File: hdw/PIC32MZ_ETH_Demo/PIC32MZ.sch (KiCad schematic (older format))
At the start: 1 part

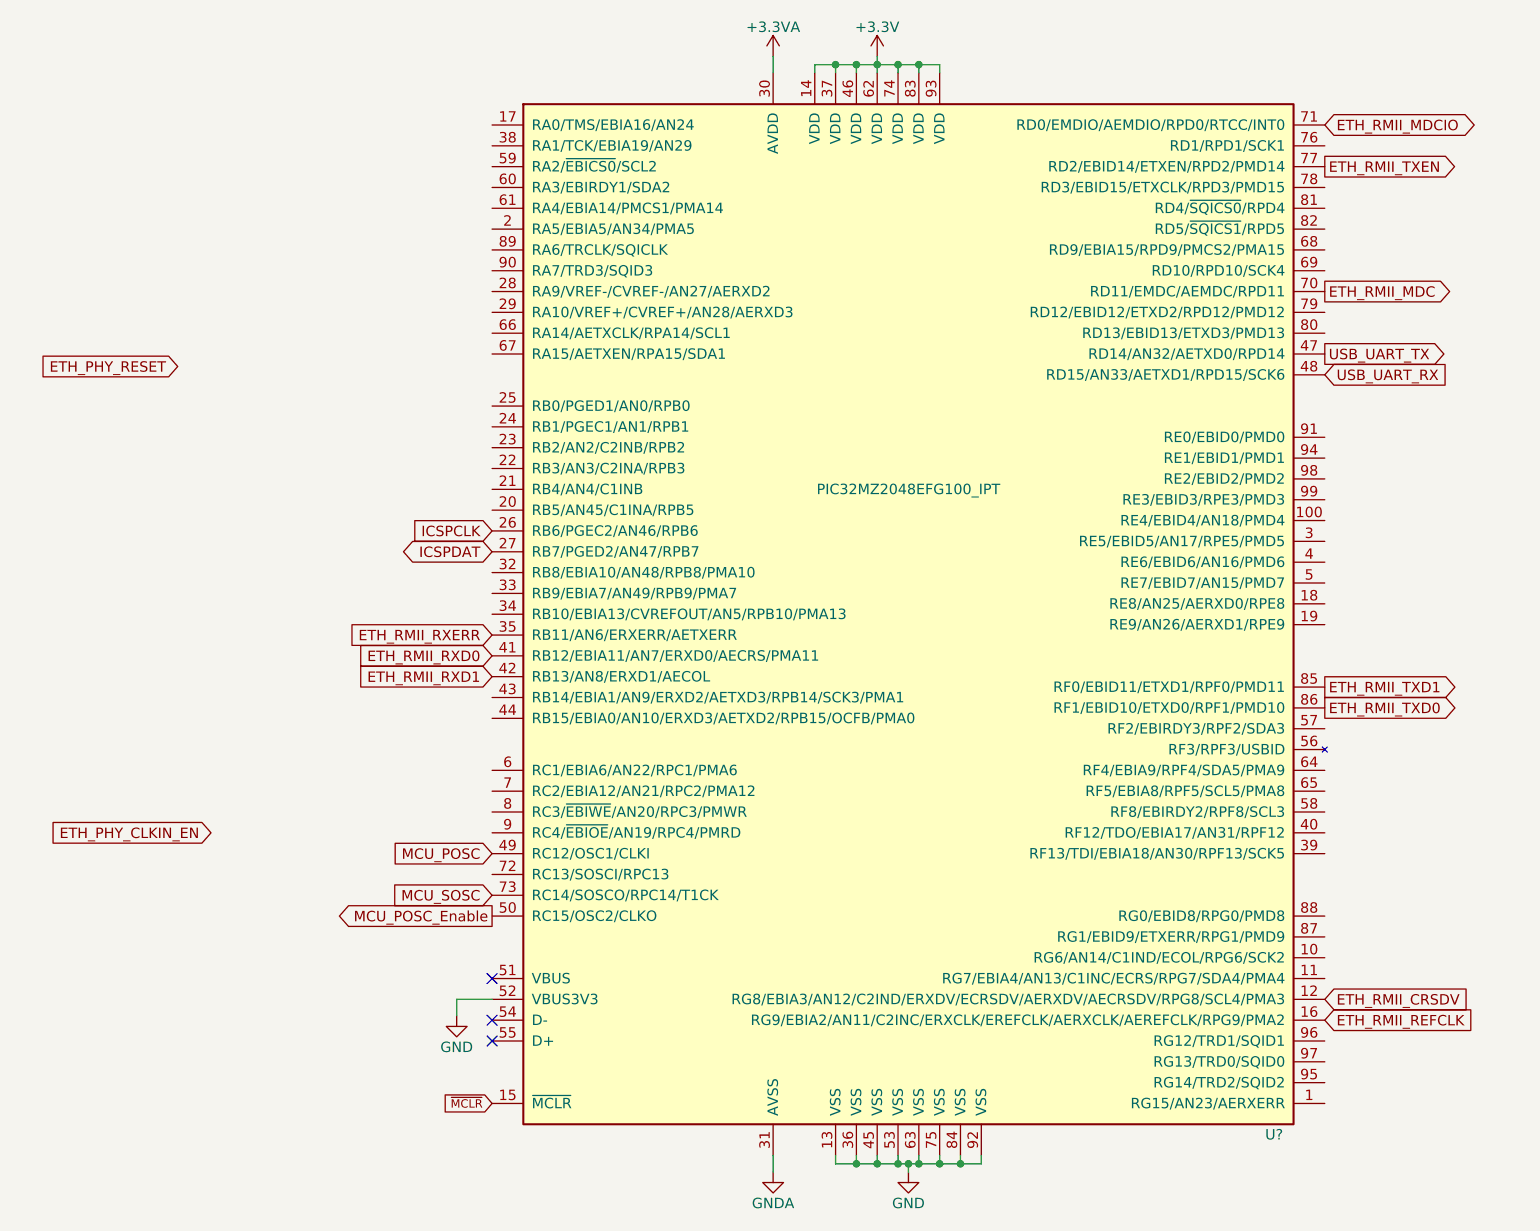
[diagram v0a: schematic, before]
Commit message: More schematic tweaks, followed PHY design guide
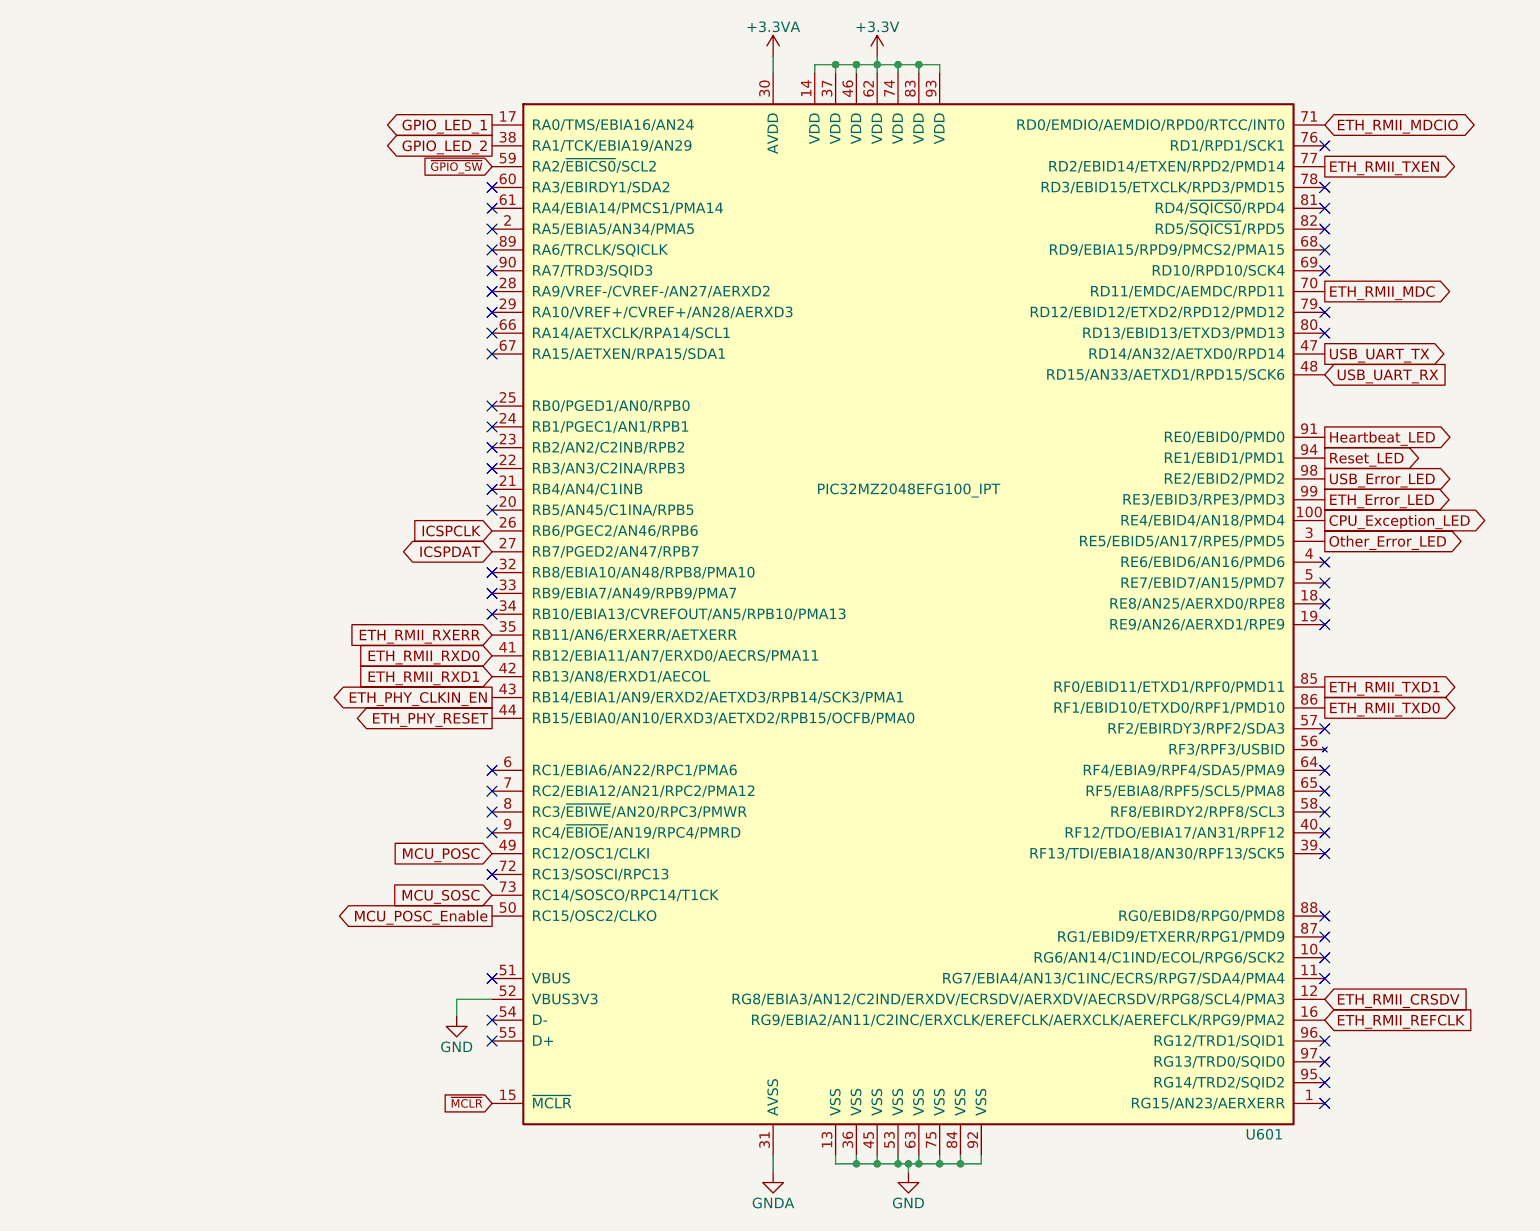
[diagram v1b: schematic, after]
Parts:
- gave numbers to parts that had none: 1
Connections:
- net ETH_PHY_CLKIN_EN: now also U601.43 (RB14/EBIA1/AN9/ERXD2/AETXD3/RPB14/SCK3/PMA1)
- net ETH_PHY_RESET: now also U601.44 (RB15/EBIA0/AN10/ERXD3/AETXD2/RPB15/OCFB/PMA0)
- net CPU_Exception_LED: now reaches U601.100 (RE4/EBID4/AN18/PMD4)
- net GPIO_LED_1: now reaches U601.17 (RA0/TMS/EBIA16/AN24)
- net Other_Error_LED: now reaches U601.3 (RE5/EBID5/AN17/RPE5/PMD5)
- net GPIO_LED_2: now reaches U601.38 (RA1/TCK/EBIA19/AN29)
- net ~GPIO_SW: now reaches U601.59 (RA2/~EBICS0~/SCL2)
- net Heartbeat_LED: now reaches U601.91 (RE0/EBID0/PMD0)
- net Reset_LED: now reaches U601.94 (RE1/EBID1/PMD1)
- net USB_Error_LED: now reaches U601.98 (RE2/EBID2/PMD2)
- net ETH_Error_LED: now reaches U601.99 (RE3/EBID3/RPE3/PMD3)
- no-connect marks 3 -> 52
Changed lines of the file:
@@
 EESchema Schematic File Version 4
+LIBS:PIC32MZ_ETH_Demo-cache
 EELAYER 30 0
 EELAYER END
@@
 	5510 920  5410 920
 $Comp
-L power:GND #PWR?
+L power:GND #PWR0605
 U 1 1 5CB03EF2
 P 5460 6240
-F 0 "#PWR?" H 5460 5990 50  0001 C CNN
+F 0 "#PWR0605" H 5460 5990 50  0001 C CNN
 F 1 "GND" H 5460 6090 50  0000 C CNN
 F 2 "" H 5460 6240 50  0001 C CNN
@@
 	5710 6200 5810 6200
 $Comp
-L power:GNDA #PWR?
+L power:GNDA #PWR0603
 U 1 1 5CB07CEA
 P 4810 6240
-F 0 "#PWR?" H 4810 5990 50  0001 C CNN
+F 0 "#PWR0603" H 4810 5990 50  0001 C CNN
 F 1 "GNDA" H 4810 6090 50  0000 C CNN
 F 2 "" H 4810 6240 50  0001 C CNN
@@
 	4810 6160 4810 6240
 $Comp
-L power:+3.3VA #PWR?
+L power:+3.3VA #PWR0602
 U 1 1 5CB087D9
 P 4810 880
-F 0 "#PWR?" H 4810 730 50  0001 C CNN
+F 0 "#PWR0602" H 4810 730 50  0001 C CNN
 F 1 "+3.3VA" H 4810 1020 50  0000 C CNN
 F 2 "" H 4810 880 50  0001 C CNN
@@
 NoConn ~ 3460 5310
 $Comp
-L power:GND #PWR?
+L power:GND #PWR0601
 U 1 1 5CB14B21
 P 3290 5490
-F 0 "#PWR?" H 3290 5240 50  0001 C CNN
+F 0 "#PWR0601" H 3290 5240 50  0001 C CNN
 F 1 "GND" H 3290 5340 50  0000 C CNN
 F 2 "" H 3290 5490 50  0001 C CNN
@@
 USB_UART_TX
 $Comp
-L Custom_Library:PIC32MZ2048EFG100_IPT U?
+L Custom_Library:PIC32MZ2048EFG100_IPT U601
 U 1 1 5E6CE439
 P 5460 3560
-F 0 "U?" H 7260 1060 50  0000 R CNN
+F 0 "U601" H 7260 1060 50  0000 R CNN
 F 1 "PIC32MZ2048EFG100_IPT" H 5460 4160 50  0000 C CNN
 F 2 "Housings_QFP:TQFP-100_14x14mm_Pitch0.5mm" H 5460 3560 50  0001 C CNN
@@
 $EndComp
 $Comp
-L power:+3.3V #PWR?
+L power:+3.3V #PWR0604
 U 1 1 5E6E7B25
 P 5310 880
-F 0 "#PWR?" H 5310 730 50  0001 C CNN
+F 0 "#PWR0604" H 5310 730 50  0001 C CNN
 F 1 "+3.3V" H 5310 1020 50  0000 C CNN
 F 2 "" H 5310 880 50  0001 C CNN
@@
 Text GLabel 7460 4010 2    50   Output ~ 0
 ETH_RMII_TXD0
-Text GLabel 2110 4610 0    50   Input ~ 0
+Text GLabel 3460 3960 0    50   Output ~ 0
 ETH_PHY_CLKIN_EN
-Text GLabel 1950 2370 0    50   Input ~ 0
+Text GLabel 3460 4060 0    50   Output ~ 0
 ETH_PHY_RESET
+Text GLabel 3460 1410 0    40   Input ~ 0
+~GPIO_SW
+Text GLabel 3460 1210 0    50   Output ~ 0
+GPIO_LED_1
+Text GLabel 3460 1310 0    50   Output ~ 0
+GPIO_LED_2
+Text GLabel 7460 2710 2    50   Output ~ 0
+Heartbeat_LED
+Text GLabel 7460 2810 2    50   Output ~ 0
+Reset_LED
+Text GLabel 7460 2910 2    50   Output ~ 0
+USB_Error_LED
+Text GLabel 7460 3010 2    50   Output ~ 0
+ETH_Error_LED
+Text GLabel 7460 3210 2    50   Output ~ 0
+Other_Error_LED
+Text GLabel 7460 3110 2    50   Output ~ 0
+CPU_Exception_LED
+NoConn ~ 3460 1510
+NoConn ~ 3460 1610
+NoConn ~ 3460 1710
+NoConn ~ 3460 1810
+NoConn ~ 3460 1910
+NoConn ~ 3460 2010
+NoConn ~ 3460 2110
+NoConn ~ 3460 2210
+NoConn ~ 3460 2310
+NoConn ~ 3460 2560
+NoConn ~ 3460 2660
+NoConn ~ 3460 2760
+NoConn ~ 3460 2860
+NoConn ~ 3460 2960
+NoConn ~ 3460 3060
+NoConn ~ 3460 3360
+NoConn ~ 3460 3460
+NoConn ~ 3460 3560
+NoConn ~ 3460 4310
+NoConn ~ 3460 4410
+NoConn ~ 3460 4510
+NoConn ~ 3460 4610
+NoConn ~ 3460 4810
+NoConn ~ 7460 1310
+NoConn ~ 7460 1510
+NoConn ~ 7460 1610
+NoConn ~ 7460 1710
+NoConn ~ 7460 1810
+NoConn ~ 7460 1910
+NoConn ~ 7460 2110
+NoConn ~ 7460 2210
+NoConn ~ 7460 3310
+NoConn ~ 7460 3410
+NoConn ~ 7460 3510
+NoConn ~ 7460 3610
+NoConn ~ 7460 4110
+NoConn ~ 7460 4310
+NoConn ~ 7460 4410
+NoConn ~ 7460 4510
+NoConn ~ 7460 4610
+NoConn ~ 7460 4710
+NoConn ~ 7460 5010
+NoConn ~ 7460 5110
+NoConn ~ 7460 5210
+NoConn ~ 7460 5310
+NoConn ~ 7460 5610
+NoConn ~ 7460 5710
+NoConn ~ 7460 5810
+NoConn ~ 7460 5910
 $EndSCHEMATC

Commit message: Finished board layout
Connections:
- net CPU_Exception_LED: now also U601.9 (RC4/~EBIOE~/AN19/RPC4/PMRD); no longer U601.100 (RE4/EBID4/AN18/PMD4)
- net ETH_Error_LED: now also U601.6 (RC1/EBIA6/AN22/RPC1/PMA6); no longer U601.99 (RE3/EBID3/RPE3/PMD3)
- net ETH_PHY_CLKIN_EN: now also U601.81 (RD4/~SQICS0~/RPD4); no longer U601.43 (RB14/EBIA1/AN9/ERXD2/AETXD3/RPB14/SCK3/PMA1)
- net ETH_PHY_RESET: now also U601.60 (RA3/EBIRDY1/SDA2); no longer U601.44 (RB15/EBIA0/AN10/ERXD3/AETXD2/RPB15/OCFB/PMA0)
- net GPIO_LED_1: now also U601.58 (RF8/EBIRDY2/RPF8/SCL3); no longer U601.17 (RA0/TMS/EBIA16/AN24)
- net GPIO_LED_2: now also U601.57 (RF2/EBIRDY3/RPF2/SDA3); no longer U601.38 (RA1/TCK/EBIA19/AN29)
- net Heartbeat_LED: now also U601.11 (RG7/EBIA4/AN13/C1INC/ECRS/RPG7/SDA4/PMA4); no longer U601.91 (RE0/EBID0/PMD0)
- net Other_Error_LED: now also U601.7 (RC2/EBIA12/AN21/RPC2/PMA12); no longer U601.3 (RE5/EBID5/AN17/RPE5/PMD5)
- net Reset_LED: now also U601.10 (RG6/AN14/C1IND/ECOL/RPG6/SCK2); no longer U601.94 (RE1/EBID1/PMD1)
- net USB_Error_LED: now also U601.8 (RC3/~EBIWE~/AN20/RPC3/PMWR); no longer U601.98 (RE2/EBID2/PMD2)
- net ~GPIO_SW: now also U601.44 (RB15/EBIA0/AN10/ERXD3/AETXD2/RPB15/OCFB/PMA0); no longer U601.59 (RA2/~EBICS0~/SCL2)
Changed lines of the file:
@@
 Text GLabel 7460 4010 2    50   Output ~ 0
 ETH_RMII_TXD0
-Text GLabel 3460 3960 0    50   Output ~ 0
+Text GLabel 7460 1610 2    50   Output ~ 0
 ETH_PHY_CLKIN_EN
-Text GLabel 3460 4060 0    50   Output ~ 0
+Text GLabel 3460 1510 0    50   Output ~ 0
 ETH_PHY_RESET
-Text GLabel 3460 1410 0    40   Input ~ 0
+Text GLabel 3460 4060 0    40   Input ~ 0
 ~GPIO_SW
-Text GLabel 3460 1210 0    50   Output ~ 0
+Text GLabel 7460 4510 2    50   Output ~ 0
 GPIO_LED_1
-Text GLabel 3460 1310 0    50   Output ~ 0
+Text GLabel 7460 4110 2    50   Output ~ 0
 GPIO_LED_2
-Text GLabel 7460 2710 2    50   Output ~ 0
+Text GLabel 7460 5310 2    50   Output ~ 0
 Heartbeat_LED
-Text GLabel 7460 2810 2    50   Output ~ 0
+Text GLabel 7460 5210 2    50   Output ~ 0
 Reset_LED
-Text GLabel 7460 2910 2    50   Output ~ 0
+Text GLabel 3460 4510 0    50   Output ~ 0
 USB_Error_LED
-Text GLabel 7460 3010 2    50   Output ~ 0
+Text GLabel 3460 4310 0    50   Output ~ 0
 ETH_Error_LED
-Text GLabel 7460 3210 2    50   Output ~ 0
+Text GLabel 3460 4410 0    50   Output ~ 0
 Other_Error_LED
-Text GLabel 7460 3110 2    50   Output ~ 0
+Text GLabel 3460 4610 0    50   Output ~ 0
 CPU_Exception_LED
-NoConn ~ 3460 1510
 NoConn ~ 3460 1610
 NoConn ~ 3460 1710
@@
 NoConn ~ 3460 3460
 NoConn ~ 3460 3560
-NoConn ~ 3460 4310
-NoConn ~ 3460 4410
-NoConn ~ 3460 4510
-NoConn ~ 3460 4610
 NoConn ~ 3460 4810
 NoConn ~ 7460 1310
 NoConn ~ 7460 1510
-NoConn ~ 7460 1610
 NoConn ~ 7460 1710
 NoConn ~ 7460 1810
@@
 NoConn ~ 7460 3510
 NoConn ~ 7460 3610
-NoConn ~ 7460 4110
 NoConn ~ 7460 4310
 NoConn ~ 7460 4410
-NoConn ~ 7460 4510
 NoConn ~ 7460 4610
 NoConn ~ 7460 4710
 NoConn ~ 7460 5010
 NoConn ~ 7460 5110
-NoConn ~ 7460 5210
-NoConn ~ 7460 5310
 NoConn ~ 7460 5610
 NoConn ~ 7460 5710
 NoConn ~ 7460 5810
 NoConn ~ 7460 5910
+NoConn ~ 7460 2710
+NoConn ~ 7460 2810
+NoConn ~ 7460 2910
+NoConn ~ 7460 3010
+NoConn ~ 7460 3110
+NoConn ~ 7460 3210
+NoConn ~ 3460 3960
+NoConn ~ 3460 1210
+NoConn ~ 3460 1310
+NoConn ~ 3460 1410
 $EndSCHEMATC
